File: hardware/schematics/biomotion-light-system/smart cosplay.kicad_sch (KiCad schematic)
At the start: 27 parts, among them J1 USB_C_Receptacle_USB2.0_14P

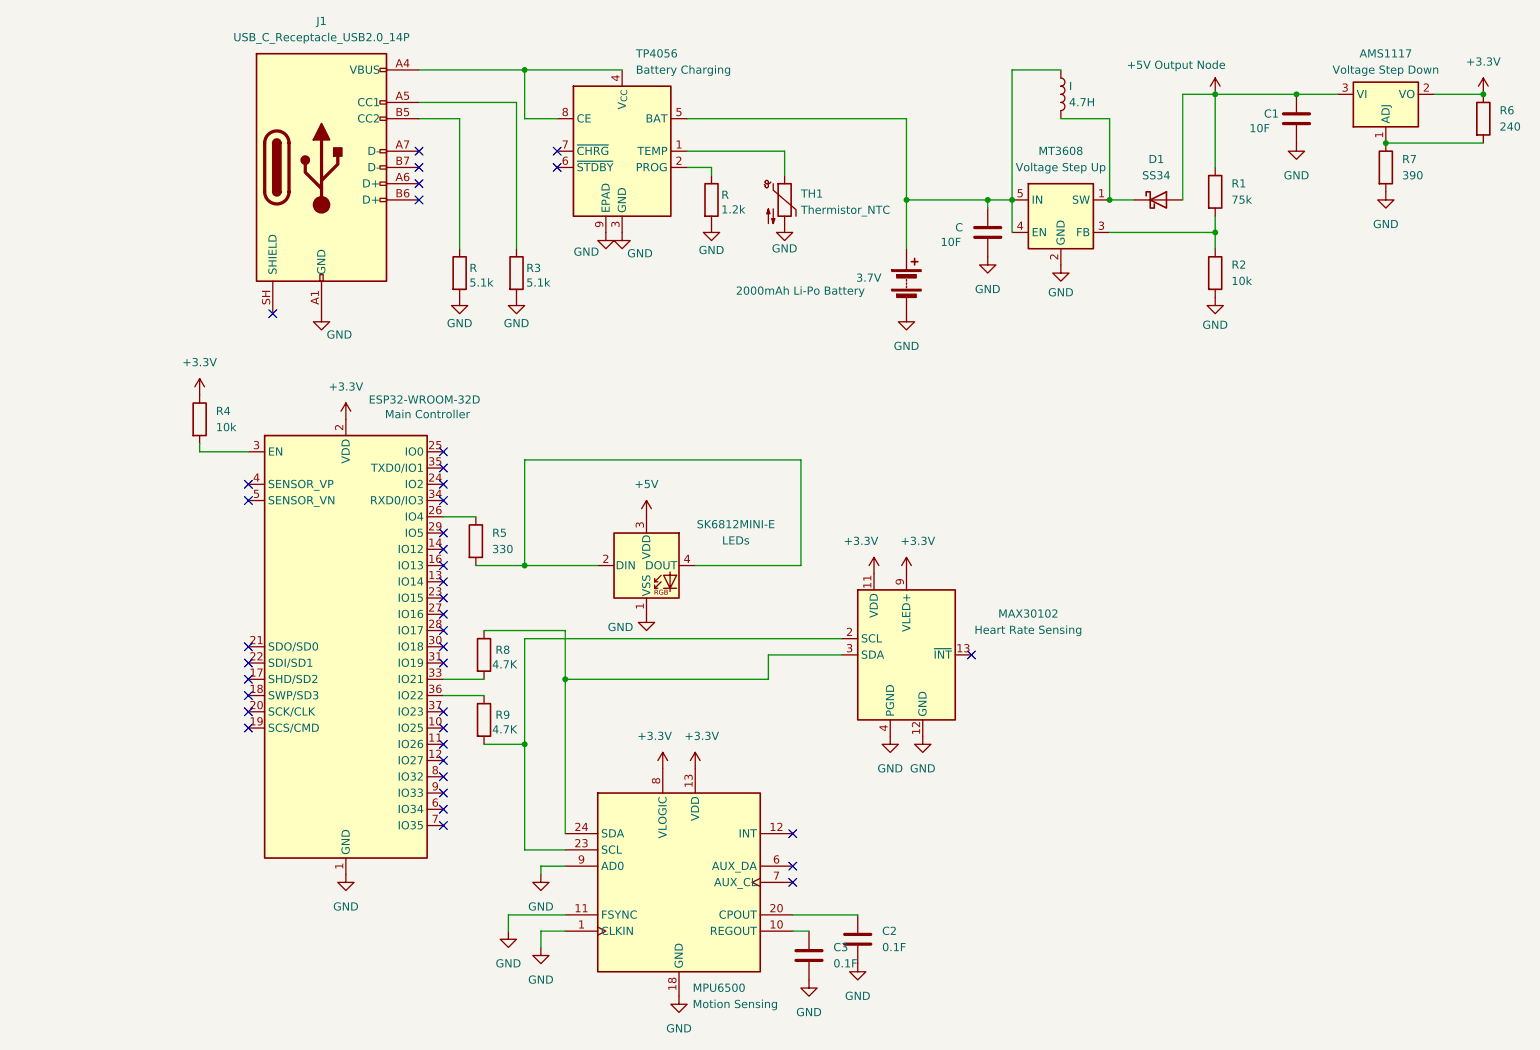
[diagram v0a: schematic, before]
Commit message: cleanup: code typos, slight changes to pulse animation, and docs
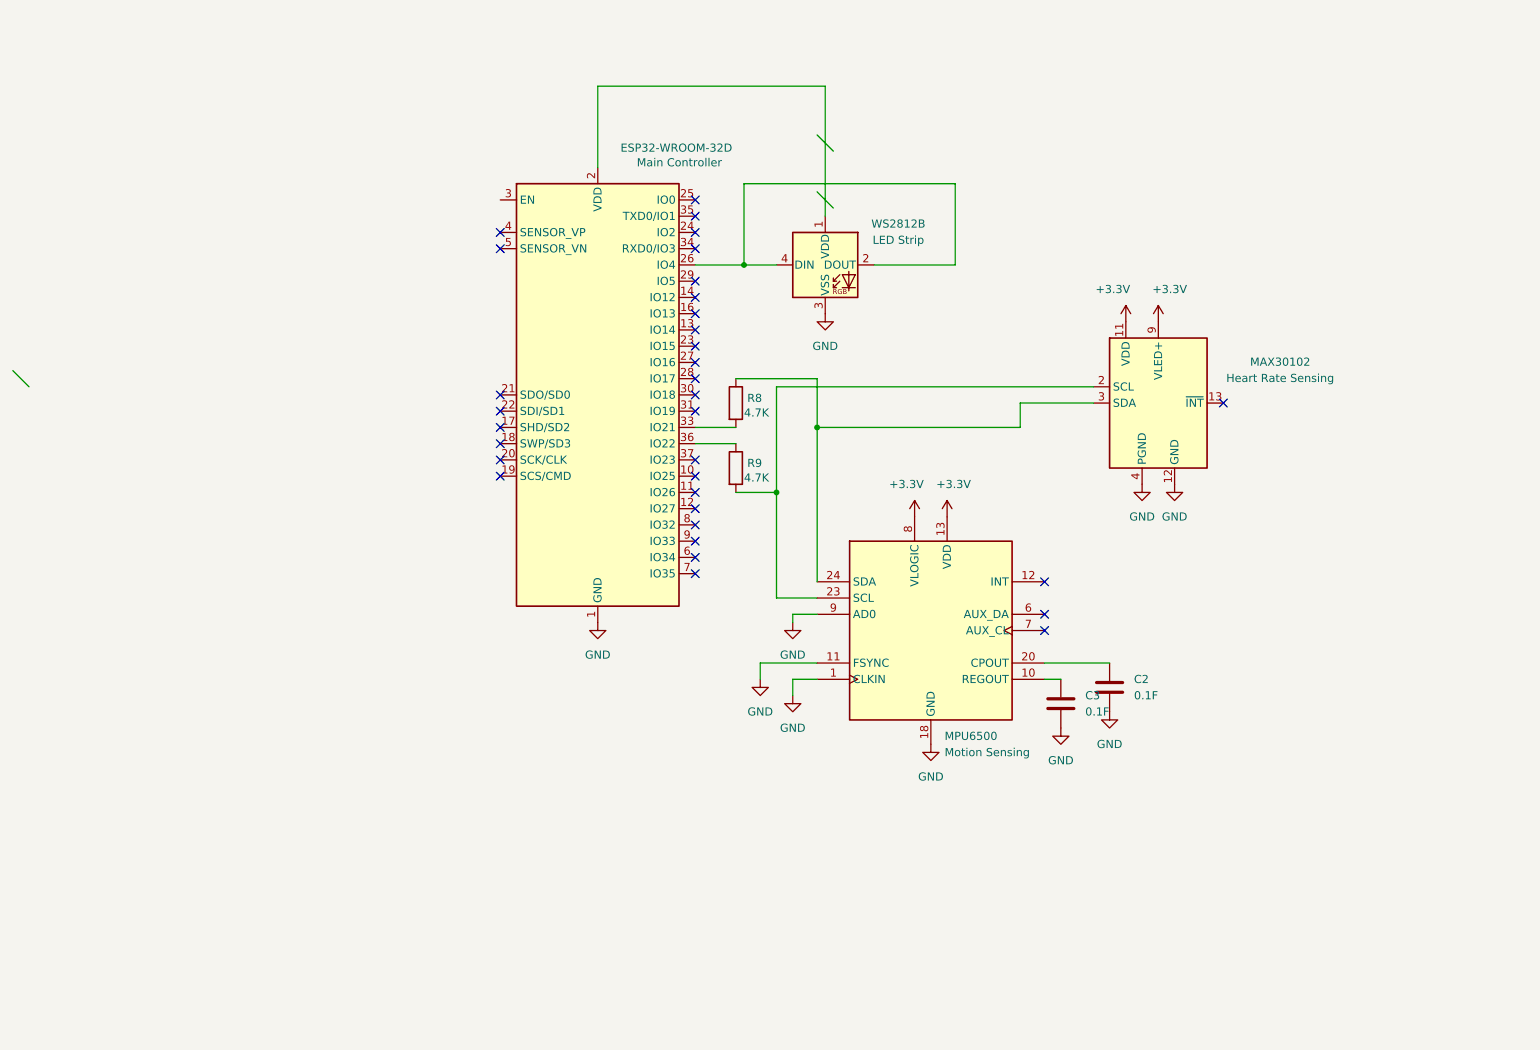
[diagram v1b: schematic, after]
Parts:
- removed 3.7V: 2000mAh Li-Po Battery, symbol Device:Battery
- removed AMS1117: Voltage Step Down, Package_TO_SOT_SMD:SOT-223-3_TabPin2, symbol Regulator_Linear:AMS1117
- removed C, C1: 10F, symbol Device:C
- removed D1: SS34, Diode_SMD:D_SMA, symbol Diode:SS34
- removed I: 4.7H, symbol Device:L
- removed J1: USB_C_Receptacle_USB2.0_14P, symbol Connector:USB_C_Receptacle_USB2.0_14P
- removed MT3608: Voltage Step Up, Package_TO_SOT_SMD:SOT-23-6, symbol Regulator_Switching:MT3608
- removed R, R3: 5.1k, symbol Device:R
- removed R: 1.2k, symbol Device:R
- removed R1: 75k, symbol Device:R
- removed R2, R4: 10k, symbol Device:R
- removed R5: 330, symbol Device:R
- removed R6: 240, symbol Device:R
- removed R7: 390, symbol Device:R
- removed SK6812MINI-E: LEDs, LED_SMD:LED_SK6812MINI-E_3.2x2.8mm_P1.5mm_ReverseMount, symbol LED:SK6812MINI-E
- removed TH1: Thermistor_NTC, symbol Device:Thermistor_NTC
- removed TP4056: Battery Charging, Package_SO:SOIC-8-1EP_3.9x4.9mm_P1.27mm_EP2.41x3.3mm_ThermalVias, symbol Battery_Management:TP4056-42-ESOP8
- added WS2812B: LED Strip, LED_SMD:LED_WS2812B_PLCC4_5.0x5.0mm_P3.2mm, symbol LED:WS2812B
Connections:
- net +3.3V: no longer ESP32-WROOM-32D.2 (VDD)
- net GND: now also WS2812B.3 (VSS)
- net at ESP32-WROOM-32D.26 (IO4): now also WS2812B.2 (DOUT), WS2812B.4 (DIN)
- new net: ESP32-WROOM-32D.2 (VDD), WS2812B.1 (VDD)
- no-connect marks 40 -> 33
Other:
- moved on the sheet: C2, C3, ESP32-WROOM-32D, MAX30102, MPU6500, R8, R9
